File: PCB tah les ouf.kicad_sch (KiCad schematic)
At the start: 19 parts, among them J1 USB_C_Receptacle_USB2.0_16P, U1 ESP32-S3-WROOM-1, U2 TMC2209_SILENTSTEPSTICK, U3 TMC2209_SILENTSTEPSTICK, U4 TMC2209_SILENTSTEPSTICK, U5 TMC2209_SILENTSTEPSTICK, U6 D3V3XA4B10LP, U7 AMS1117-3.3

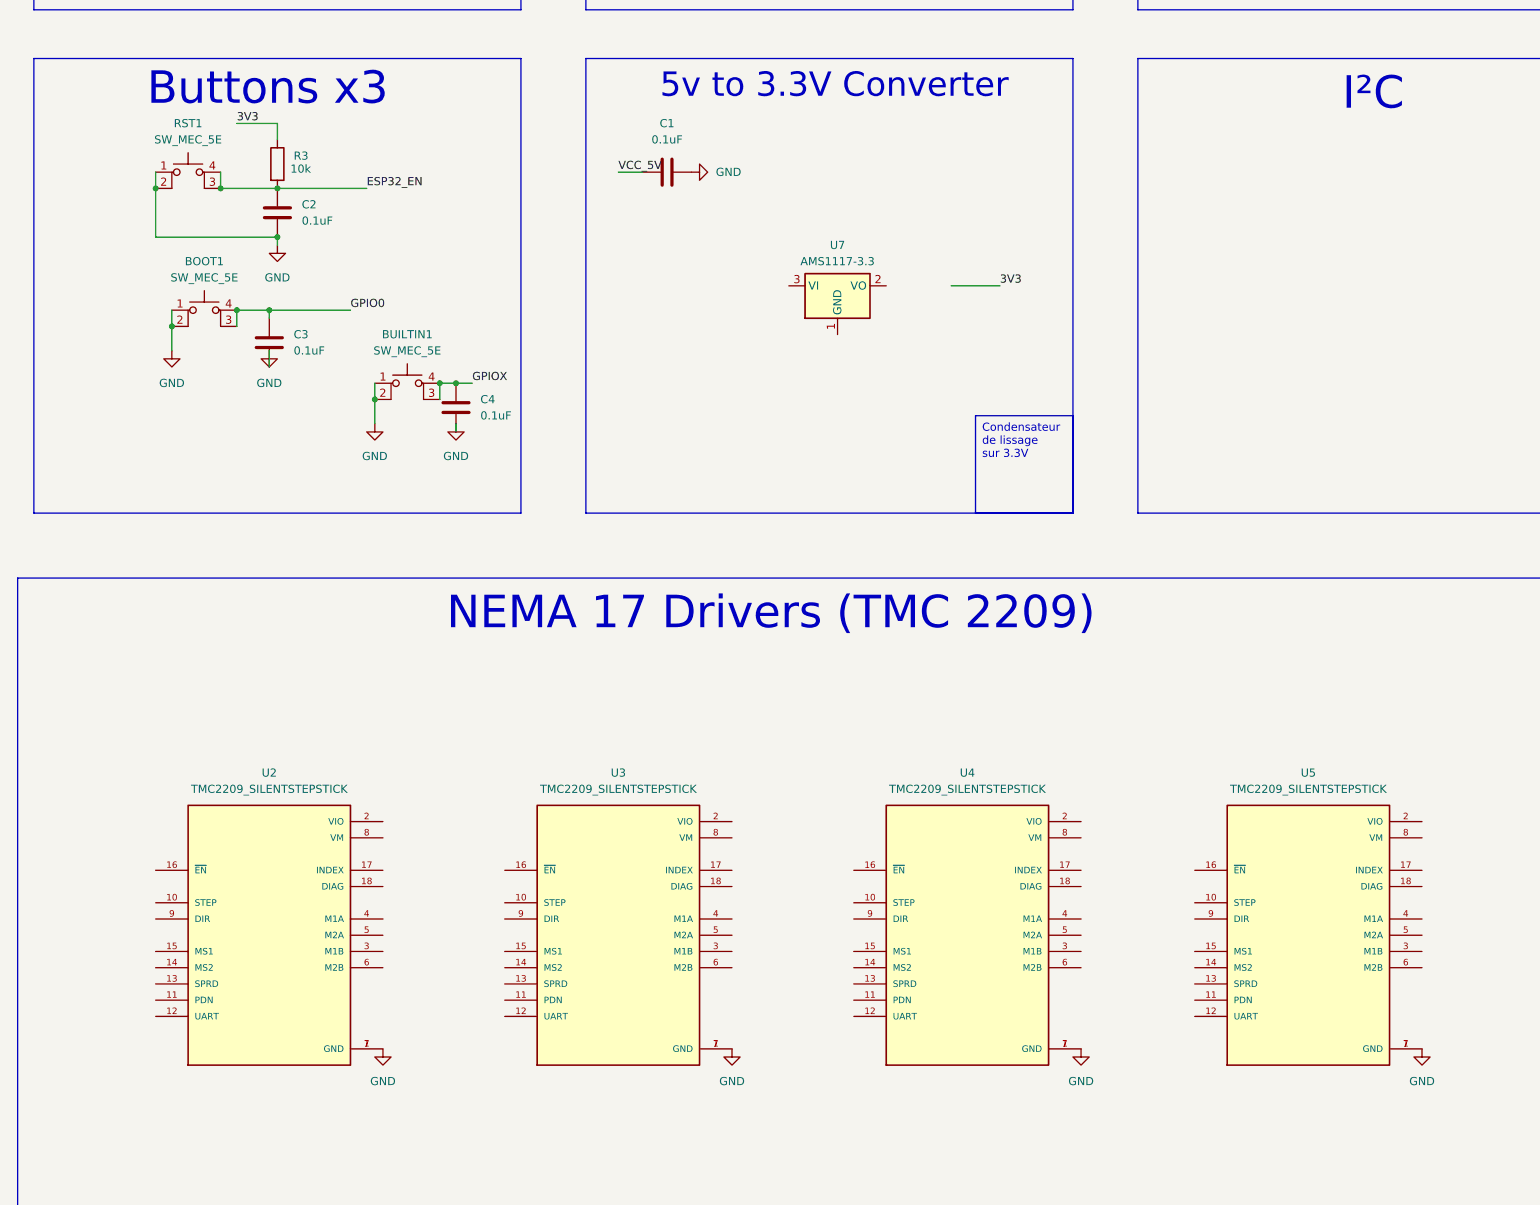
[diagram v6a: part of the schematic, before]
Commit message: Ajout switches DIP drivers & 5 to 3.3 converter
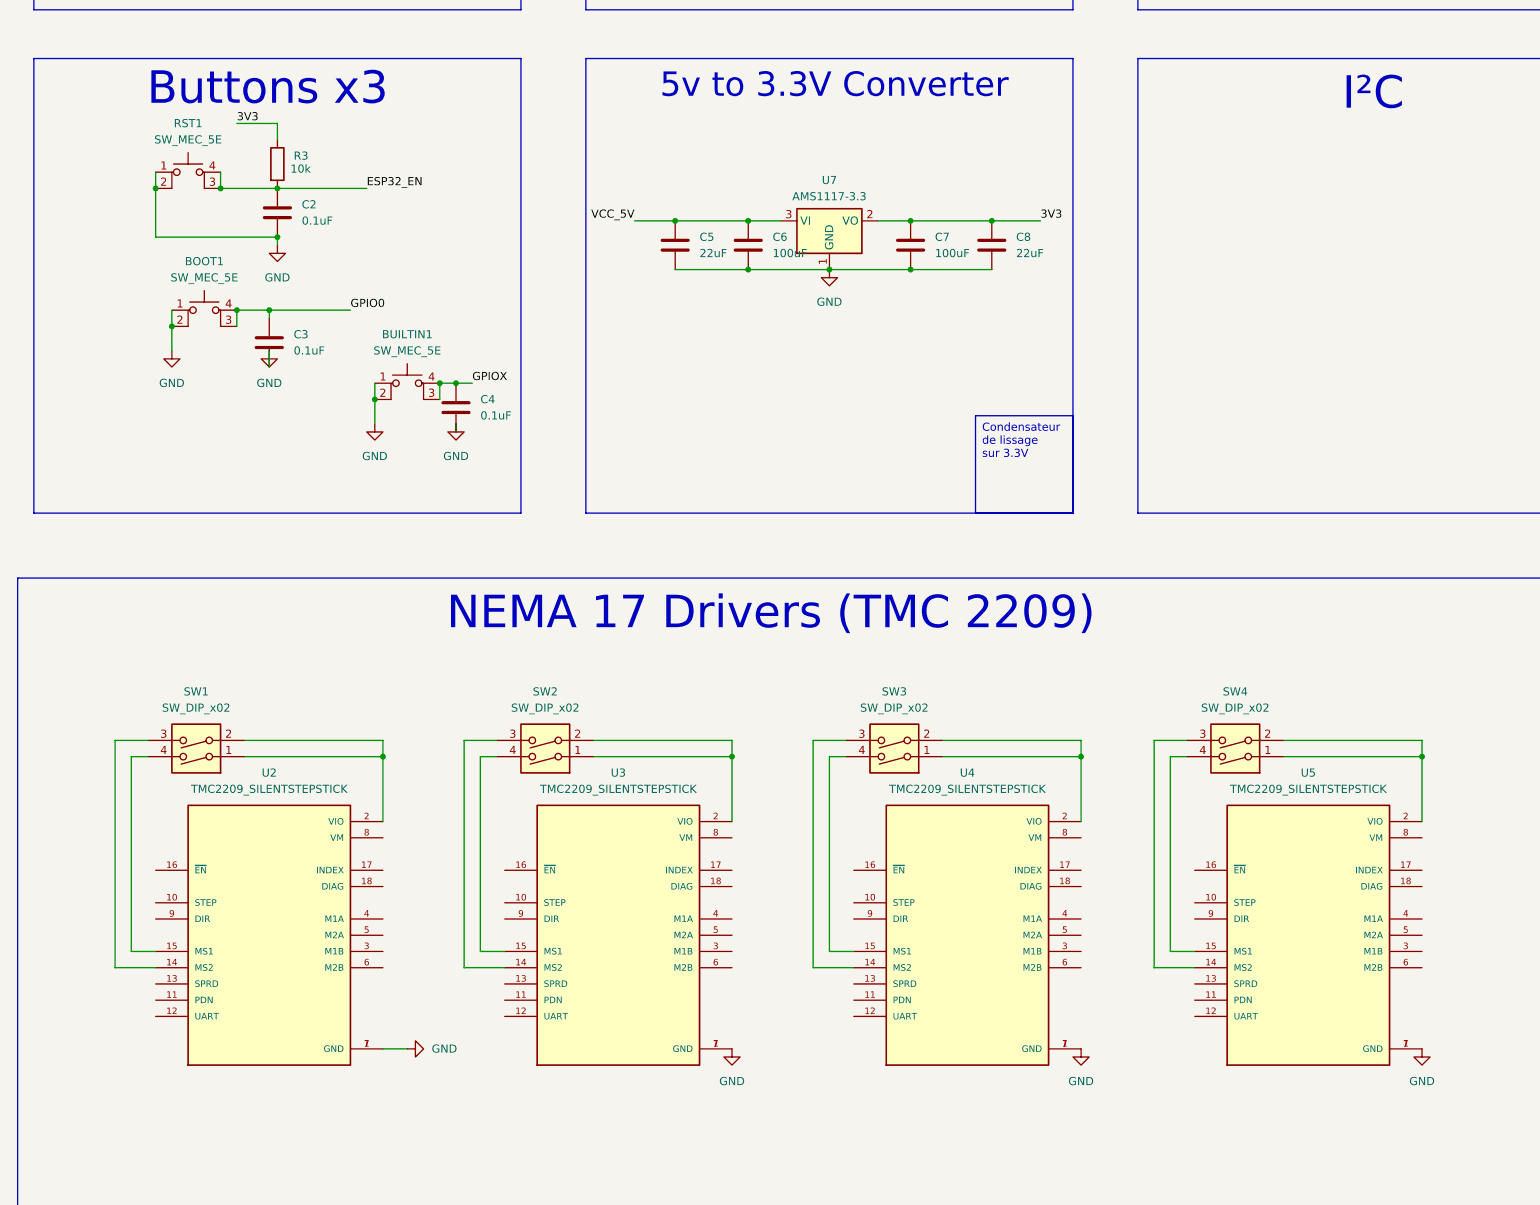
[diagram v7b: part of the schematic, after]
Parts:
- removed C1: 0.1uF, symbol Device:C
- added C5, C8: 22uF, symbol Device:C
- added C6, C7: 100uF, symbol Device:C
- added SW1, SW2, SW3, SW4: SW_DIP_x02, symbol Switch:SW_DIP_x02
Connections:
- net 3V3: now also U7.2 (VO), C7.1, C8.1
- net GND: now also U7.1 (GND), C5.2, C6.2, C7.2, C8.2
- net VCC_5V: now also U7.3 (VI), C5.1, C6.1
- net at U5.14 (MS2): now also SW4.3
- net at U5.15 (MS1): now also SW4.4
- net at U5.2 (VIO): now also SW4.1, SW4.2
- net at U2.14 (MS2): now also SW1.3
- net at U2.15 (MS1): now also SW1.4
- net at U2.2 (VIO): now also SW1.1, SW1.2
- net at U4.14 (MS2): now also SW3.3
- net at U4.15 (MS1): now also SW3.4
- net at U4.2 (VIO): now also SW3.1, SW3.2
- net at U3.14 (MS2): now also SW2.3
- net at U3.15 (MS1): now also SW2.4
- net at U3.2 (VIO): now also SW2.1, SW2.2
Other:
- moved on the sheet: U7

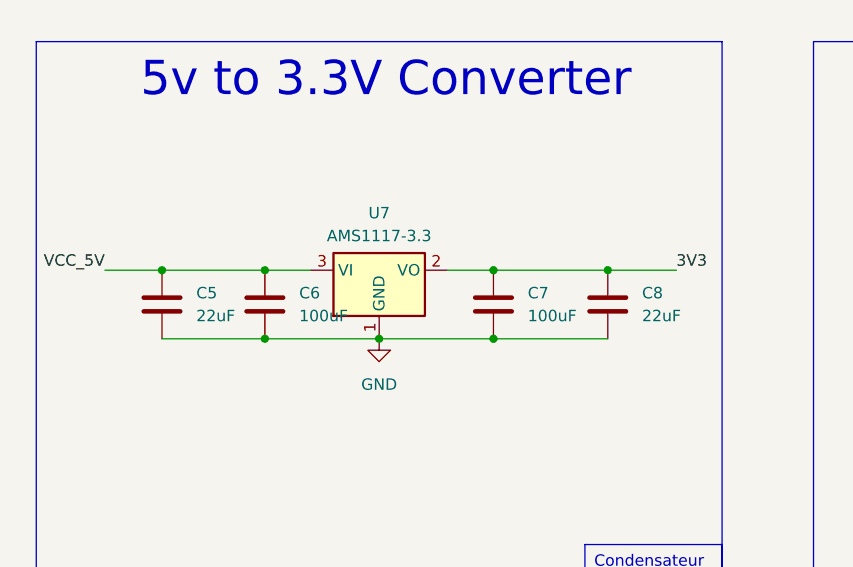
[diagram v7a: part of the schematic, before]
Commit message: Fix 5 to 3.3 converter
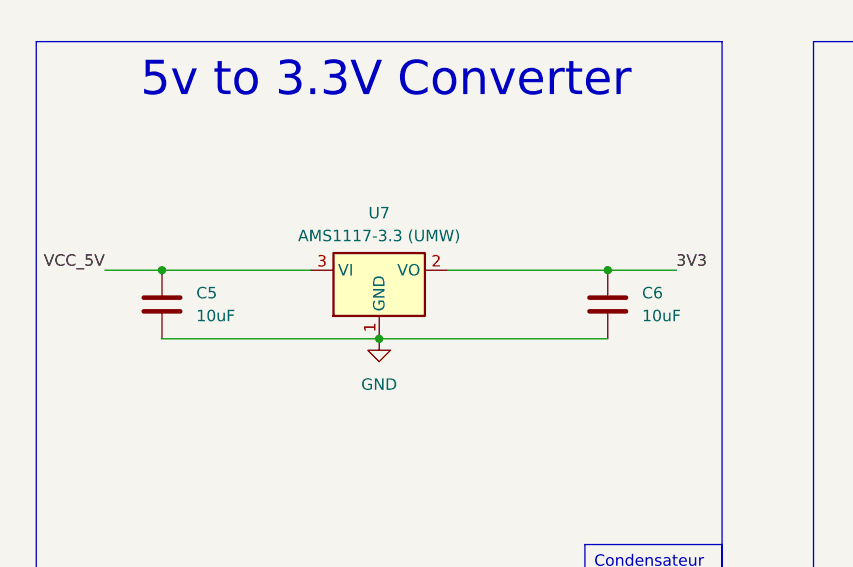
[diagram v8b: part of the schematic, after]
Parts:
- removed C6, C7: 100uF, symbol Device:C
- C5: value 22uF -> 10uF
- C6: renamed from C8; value 22uF -> 10uF
- U7: value AMS1117-3.3 -> AMS1117-3.3 (UMW)
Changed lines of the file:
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@@
 	)
 	(junction
-		(at 127 134.62)
-		(diameter 0)
-		(color 0 0 0 0)
-	)
-	(junction
 		(at 127 52.07)
 		(diameter 0)
@@
 	)
 	(junction
-		(at 152.4 127)
-		(diameter 0)
-		(color 0 0 0 0)
-	)
-	(junction
 		(at 48.26 82.55)
 		(diameter 0)
@@
 	)
 	(junction
-		(at 127 127)
-		(diameter 0)
-		(color 0 0 0 0)
-	)
-	(junction
 		(at 165.1 127)
 		(diameter 0)
@@
 	)
 	(junction
-		(at 152.4 134.62)
-		(diameter 0)
-		(color 0 0 0 0)
-	)
-	(junction
 		(at 68.58 154.94)
 		(diameter 0)
@@
 	(wire
 		(pts
-			(xy 147.32 127) (xy 152.4 127)
-		)
-		(stroke
-			(width 0)
-			(type default)
-		)
-	)
-	(wire
-		(pts
 			(xy 196.85 243.84) (xy 190.5 243.84)
 		)
@@
 	(wire
 		(pts
-			(xy 115.57 127) (xy 127 127)
+			(xy 115.57 127) (xy 132.08 127)
 		)
 		(stroke
@@
 	(wire
 		(pts
-			(xy 115.57 134.62) (xy 127 134.62)
-		)
-		(stroke
-			(width 0)
-			(type default)
-		)
-	)
-	(wire
-		(pts
 			(xy 118.11 62.23) (xy 127 62.23)
 		)
@@
 	(wire
 		(pts
-			(xy 127 127) (xy 132.08 127)
-		)
-		(stroke
-			(width 0)
-			(type default)
-		)
-	)
-	(wire
-		(pts
 			(xy 308.61 189.23) (xy 320.04 189.23)
 		)
@@
 	(wire
 		(pts
-			(xy 127 134.62) (xy 139.7 134.62)
+			(xy 115.57 134.62) (xy 139.7 134.62)
 		)
 		(stroke
@@
 	(wire
 		(pts
-			(xy 152.4 134.62) (xy 165.1 134.62)
+			(xy 139.7 134.62) (xy 165.1 134.62)
 		)
 		(stroke
@@
 	(wire
 		(pts
-			(xy 139.7 134.62) (xy 152.4 134.62)
-		)
-		(stroke
-			(width 0)
-			(type default)
-		)
-	)
-	(wire
-		(pts
 			(xy 137.16 243.84) (xy 137.16 208.28)
 		)
@@
 	(wire
 		(pts
-			(xy 152.4 127) (xy 165.1 127)
+			(xy 147.32 127) (xy 165.1 127)
 		)
 		(stroke
@@
 	)
 	(symbol
-		(lib_id "Device:C")
-		(at 152.4 130.81 0)
-		(unit 1)
-		(exclude_from_sim no)
-		(in_bom yes)
-		(on_board yes)
-		(dnp no)
-		(fields_autoplaced yes)
-		(property "Reference" "C7"
-			(at 156.21 129.5399 0)
-			(effects
-				(font
-					(size 1.27 1.27)
-				)
-				(justify left)
-			)
-		)
-		(property "Value" "100uF"
-			(at 156.21 132.0799 0)
-			(effects
-				(font
-					(size 1.27 1.27)
-				)
-				(justify left)
-			)
-		)
-		(property "Footprint" ""
-			(at 153.3652 134.62 0)
-			(effects
-				(font
-					(size 1.27 1.27)
-				)
-				(hide yes)
-			)
-		)
-		(property "Datasheet" "~"
-			(at 152.4 130.81 0)
-			(effects
-				(font
-					(size 1.27 1.27)
-				)
-				(hide yes)
-			)
-		)
-		(property "Description" "Unpolarized capacitor"
-			(at 152.4 130.81 0)
-			(effects
-				(font
-					(size 1.27 1.27)
-				)
-				(hide yes)
-			)
-		)
-		(pin "2"
-		)
-		(pin "1"
-		)
-		(instances
-			(project "PCB tah les ouf"
-				(path "/ea97f20c-9bc4-49f4-bc03-d8d68656df8b"
-					(reference "C7")
-					(unit 1)
-				)
-			)
-		)
-	)
-	(symbol
 		(lib_id "Switch:SW_DIP_x02")
 		(at 40.64 208.28 180)
@@
 	)
 	(symbol
-		(lib_id "Device:C")
-		(at 127 130.81 0)
-		(unit 1)
-		(exclude_from_sim no)
-		(in_bom yes)
-		(on_board yes)
-		(dnp no)
-		(fields_autoplaced yes)
-		(property "Reference" "C6"
-			(at 130.81 129.5399 0)
-			(effects
-				(font
-					(size 1.27 1.27)
-				)
-				(justify left)
-			)
-		)
-		(property "Value" "100uF"
-			(at 130.81 132.0799 0)
-			(effects
-				(font
-					(size 1.27 1.27)
-				)
-				(justify left)
-			)
-		)
-		(property "Footprint" ""
-			(at 127.9652 134.62 0)
-			(effects
-				(font
-					(size 1.27 1.27)
-				)
-				(hide yes)
-			)
-		)
-		(property "Datasheet" "~"
-			(at 127 130.81 0)
-			(effects
-				(font
-					(size 1.27 1.27)
-				)
-				(hide yes)
-			)
-		)
-		(property "Description" "Unpolarized capacitor"
-			(at 127 130.81 0)
-			(effects
-				(font
-					(size 1.27 1.27)
-				)
-				(hide yes)
-			)
-		)
-		(pin "2"
-		)
-		(pin "1"
-		)
-		(instances
-			(project "PCB tah les ouf"
-				(path "/ea97f20c-9bc4-49f4-bc03-d8d68656df8b"
-					(reference "C6")
-					(unit 1)
-				)
-			)
-		)
-	)
-	(symbol
 		(lib_id "TMC2209_SILENTSTEPSTICK:TMC2209_SILENTSTEPSTICK")
 		(at 214.63 238.76 0)
@@
 		(dnp no)
 		(fields_autoplaced yes)
-		(property "Reference" "C8"
+		(property "Reference" "C6"
 			(at 168.91 129.5399 0)
 			(effects
@@
 			)
 		)
-		(property "Value" "22uF"
+		(property "Value" "10uF"
 			(at 168.91 132.0799 0)
 			(effects
@@
 			(project "PCB tah les ouf"
 				(path "/ea97f20c-9bc4-49f4-bc03-d8d68656df8b"
-					(reference "C8")
+					(reference "C6")
 					(unit 1)
 				)
@@
 			)
 		)
-		(property "Value" "22uF"
+		(property "Value" "10uF"
 			(at 119.38 132.0799 0)
 			(effects
@@
 			)
 		)
-		(property "Value" "AMS1117-3.3"
+		(property "Value" "AMS1117-3.3 (UMW)"
 			(at 139.7 123.19 0)
 			(effects
@@
 			)
 		)
-		(property "Datasheet" "http://www.advanced-monolithic.com/pdf/ds1117.pdf"
+		(property "Datasheet" "https://wmsc.lcsc.com/wmsc/upload/file/pdf/v2/lcsc/2403191525_UMW-Youtai-Semiconductor-Co---Ltd--AMS1117-3-3_C347222.pdf"
 			(at 142.24 133.35 0)
 			(effects
